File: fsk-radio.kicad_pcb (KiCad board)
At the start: 4 copper layers, 62.5 x 25 mm, 82 parts, among them IC1 STM32F4xx-QFN48, IC2 AT86RF215, IC3 LM3671, IC4 LSM6DS3, IC5 CAT24-SOT23, IC7 DPX202700DT, IC8 74AHC1G04, J1 USB_A, J2 CONN_01X14, J3 CONN_02X05, J4 RF_Shield_One_Piece, J5 u.FL, J6 u.FL, J7 SMA, X1 TXETBLSANF-26, X2 32.768kHz

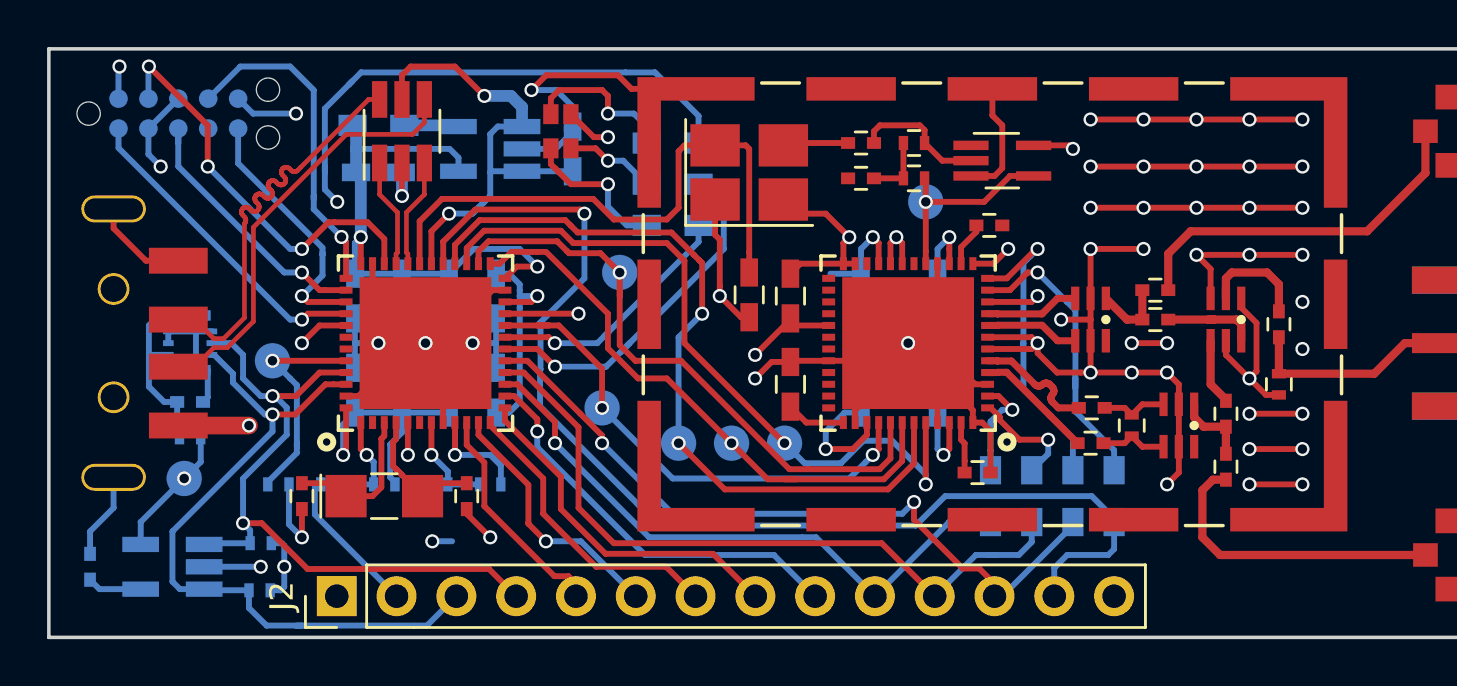
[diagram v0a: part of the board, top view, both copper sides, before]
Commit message: Cleanup silkscreen, add status LED.
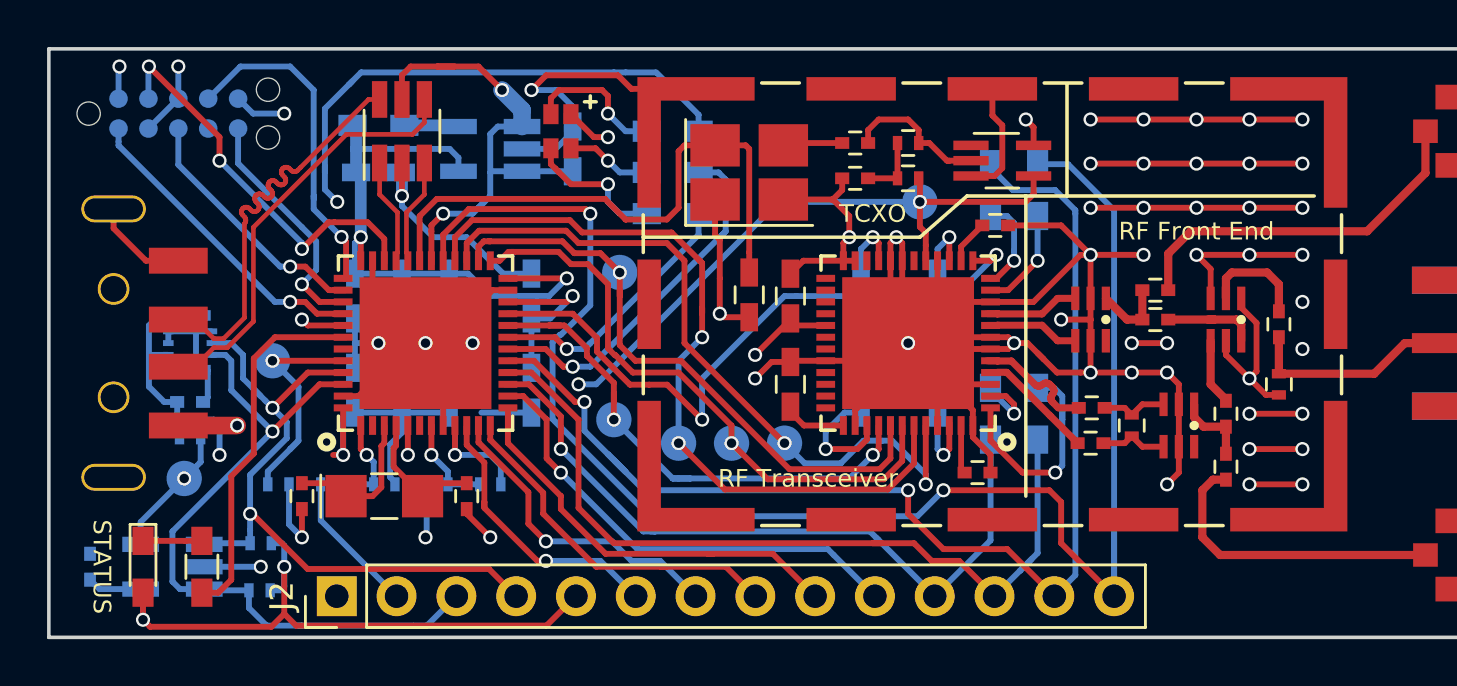
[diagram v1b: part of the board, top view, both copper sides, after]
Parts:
- added D3: LED, LEDs:LED_0603_HandSoldering, F.Cu at (101.2, 59.5)
- added R2: 270, Resistors_SMD:R_0603_HandSoldering, F.Cu at (103.8, 59.5)
- moved R15 13.5 mm to (137.2, 43.5), turned to 90 degrees
- moved R19 13.4 mm to (139.2, 43.5), turned to 90 degrees
- moved R16 3.51 mm to (139.2, 53.0)
- moved R18 3.50 mm to (137.2, 53.0)
- moved C11 1.50 mm to (117.8, 48.0), turned to 90 degrees
- moved C9 1.50 mm to (117.8, 52.0), turned to 270 degrees
- moved IRQ 0.71 mm to (121.2, 53.2)
- moved R6 0.50 mm to (123.8, 42.8)
- moved R7 0.50 mm to (123.8, 44.5)
- moved R8 0.50 mm to (123.8, 41.0)
- moved C14 0.25 mm to (131.5, 43.0)
- moved C15 0.25 mm to (131.5, 41.5)
- moved C19 0.25 mm to (137.4, 45.0)
- moved R12 0.25 mm to (133.8, 43.0)
- moved R13 0.25 mm to (133.8, 41.5)
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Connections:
- J2 pad 10: /CPU/PA5 -> /CPU/PA4
- J2 pad 11: /CPU/PA6 -> /CPU/PA5
- J2 pad 12: /CPU/PA7 -> /CPU/PA6
- J2 pad 13: /CPU/PA8 -> /CPU/PA7
- J2 pad 14: VCC -> /CPU/PA8
- J2 pad 5: /CPU/PA0 -> VCC
- J2 pad 6: /CPU/PA1 -> /CPU/PA0
- J2 pad 7: /CPU/PA2 -> /CPU/PA1
- J2 pad 8: /CPU/PA3 -> /CPU/PA2
- J2 pad 9: /CPU/PA4 -> /CPU/PA3
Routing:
- net GND: track 262.7 -> 298.2 mm, vias 53 -> 52
- net /CPU/PA7: track 31.2 -> 51.8 mm
- net /CPU/PA8: track 50.3 -> 70.4 mm, vias 1 -> 2
- net Net-(IC1-Pad42): track 0.00 -> 15.6 mm
- net /RF/FEB09: track 13.5 -> 4.18 mm
- net /RF/FEA09: track 12.6 -> 4.92 mm
- net /RF/FEA24: track 4.80 -> 9.85 mm
- net /CPU/PA6: track 30.5 -> 35.4 mm
- net /CPU/PA5: track 26.2 -> 30.9 mm
- net /CPU/PA4: track 17.4 -> 20.5 mm
- net /CPU/PA3: track 15.1 -> 17.8 mm
- net /CPU/PA2: track 12.7 -> 15.4 mm
- net Net-(C11-Pad1): track 9.60 -> 7.10 mm
- net Net-(D3-Pad1): track 0.00 -> 2.50 mm
- net Net-(IC1-Pad41): track 32.6 -> 30.1 mm
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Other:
- board text added: "A"
- board text added: "B"
- board text added: "FEx09"
- board text added: "FEx24"
- board text added: "JTAG"
- board text added: "PA7"
- board text added: "PA8"
- board text added: "RF Front End"
- board text added: "RF Transceiver"
- board text added: "STATUS"
- board text added: "TCXO"
- board text added: "https://github.com/oskirby/fsk-radio"
- board text removed: "7"
- board text removed: "8"
- board text removed: "FEA09"
- board text removed: "FEA24"
- board text removed: "FEB09"
- board text removed: "FEB24"

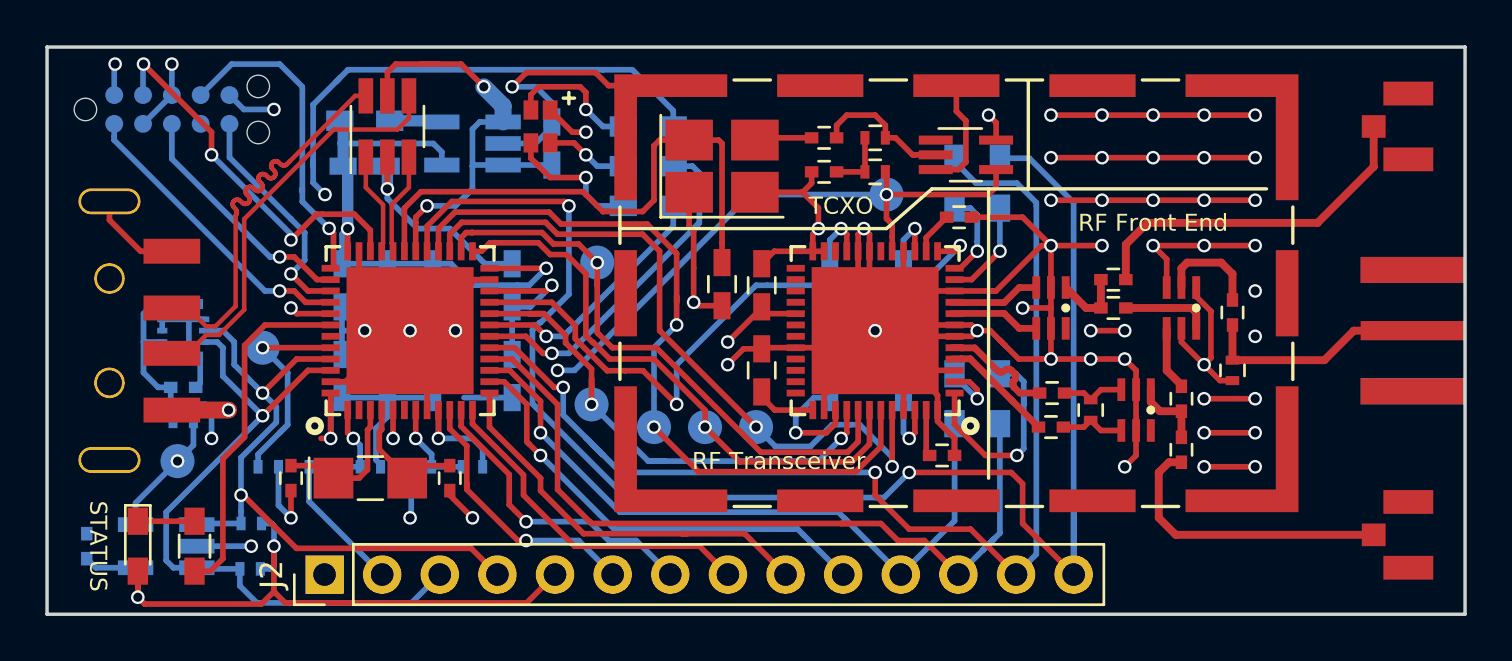
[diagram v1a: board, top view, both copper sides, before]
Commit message: Move CLKEN to BOOT1 pin to enable the TCXO during DFU boot.
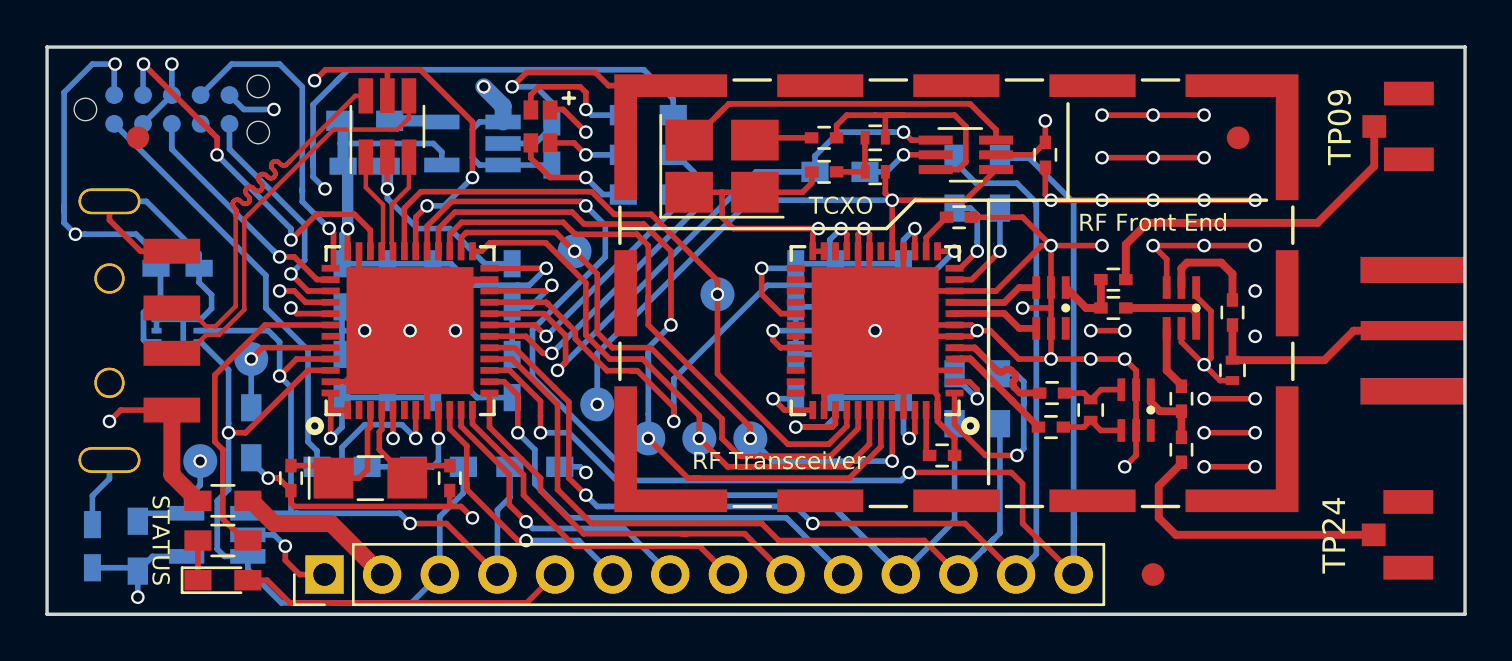
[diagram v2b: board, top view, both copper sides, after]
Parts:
- removed J5, J6: u.FL, FSK Parts:u.FL
- removed R5: 0, Resistors_SMD:R_0402
- added REF**: Fiducial_1mm_Dia_2.54mm_Outer_CopperTop, Fiducials:Fiducial_1mm_Dia_2.54mm_Outer_CopperTop, F.Cu at (101.2, 41.5)
- added REF**: Fiducial_1mm_Dia_2.54mm_Outer_CopperTop, Fiducials:Fiducial_1mm_Dia_2.54mm_Outer_CopperTop, F.Cu at (146.0, 60.8)
- added REF**: Fiducial_1mm_Dia_2.54mm_Outer_CopperTop, Fiducials:Fiducial_1mm_Dia_2.54mm_Outer_CopperTop, F.Cu at (149.8, 41.5)
- added TP09: u.FL, FSK Parts:u.FL, F.Cu at (157.3, 41.0)
- added TP24: u.FL, FSK Parts:u.FL, F.Cu at (157.2, 59.0)
- C16, C18: footprint Capacitors_SMD:C_0402 -> Capacitors_SMD:C_0603_HandSoldering
- C17: footprint Capacitors_SMD:C_0603_HandSoldering -> Capacitors_SMD:C_0402
- C21, C23: moved to B.Cu
- IC8: value 74AHC1G04 -> 74AHC2G04; footprint TO_SOT_Packages_SMD:SOT-353_SC-70-5_Handsoldering -> TO_SOT_Packages_SMD:SOT-363_SC-70-6_Handsoldering
- R1: footprint Resistors_SMD:R_0402 -> Resistors_SMD:R_0603_HandSoldering; moved to F.Cu
- R10, R11: footprint Resistors_SMD:R_0402 -> Resistors_SMD:R_0603_HandSoldering
- R14: value 4,7k -> 100k; footprint Resistors_SMD:R_0402 -> Resistors_SMD:R_0603_HandSoldering
- R3: value 0 -> 100k; footprint Resistors_SMD:R_0402 -> Resistors_SMD:R_0603_HandSoldering
- R4, R9: value 4.7k -> 100k; footprint Resistors_SMD:R_0402 -> Resistors_SMD:R_0603_HandSoldering
- moved R3 26.4 mm to (132.2, 43.0)
- moved TCXO 15.8 mm to (121.5, 53.2)
- moved C17 15.3 mm to (141.2, 42.2)
- moved R11 12.7 mm to (118.8, 56.0)
- moved R10 9.44 mm to (114.5, 56.0), turned to 0 degrees
- moved IRQ 7.37 mm to (126.8, 48.4), turned to 90 degrees
- moved R1 6.67 mm to (105.0, 57.5), turned to 180 degrees
- moved R14 5.85 mm to (101.2, 59.5), turned to 90 degrees
- moved R4 5.75 mm to (110.2, 56.0)
- moved C16 5.26 mm to (103.0, 47.2)
- moved D3 4.04 mm to (105.0, 61.0), turned to 0 degrees
- moved IC5 2.30 mm to (104.8, 59.0)
- moved R9 1.68 mm to (106.2, 54.5), turned to 270 degrees
- moved C21 1.52 mm to (130.2, 52.0)
- moved C23 1.50 mm to (130.2, 48.0), turned to 270 degrees
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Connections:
- C17 pad 2: /CPU/CLKEN -> VCC
- C4 pad 1: Net-(C4-Pad1) -> Net-(B24-Pad1)
- C4 pad 2: Net-(B24-Pad1) -> Net-(C4-Pad2)
- D2 pad 5: +5V -> Net-(D2-Pad5)
- IC1 pad 1: Net-(IC1-Pad1) -> VCC
- IC1 pad 20: /CPU/RF_IRQ -> /CPU/~CLKEN
- IC1 pad 30: +5V -> Net-(D2-Pad5)
- IC1 pad 31: /CPU/CLKEN -> /CPU/RF_IRQ
- IC8 pad 1: (no net) -> /CPU/~CLKEN
- IC8 pad 2: Net-(C15-Pad2) -> GND
- IC8 pad 3: GND -> Net-(C15-Pad2)
- J1 pad 1: +5V -> Net-(D2-Pad5)
- J3 pad 10: Net-(IC1-Pad40) -> ~NRST
- R1 pad 1: Net-(IC1-Pad1) -> +5V
- R1 pad 2: VCC -> Net-(D2-Pad5)
- R3 pad 1: Net-(IC1-Pad1) -> GND
- R3 pad 2: +5V -> /CPU/~CLKEN
- X1 pad 4: /CPU/CLKEN -> Net-(IC8-Pad6)
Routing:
- net Net-(D2-Pad5): track 0.00 -> 42.8 mm, vias 0 -> 4
- net GND: track 298.2 -> 328.8 mm, vias 52 -> 48
- net /CPU/~CLKEN: track 0.00 -> 27.5 mm, vias 0 -> 2
- net Net-(IC1-Pad40): track 29.6 -> 2.46 mm, vias 2 -> 1
- net /CPU/CLKEN: track 24.7 -> 0.00 mm
- net VCC: track 118.5 -> 142.3 mm
- net ~NRST: track 4.28 -> 26.1 mm
- net Net-(IC8-Pad6): track 0.00 -> 15.5 mm
- net +5V: track 62.8 -> 48.6 mm, vias 3 -> 1
- net Net-(C4-Pad1): track 13.0 -> 0.00 mm
- net Net-(C4-Pad2): track 0.00 -> 12.6 mm
- net /CPU/RF_IRQ: track 22.7 -> 29.7 mm, vias 2 -> 1
- net Net-(C15-Pad2): track 6.15 -> 11.5 mm
- net Net-(IC1-Pad1): track 4.15 -> 0.00 mm, vias 1 -> 0
- net Net-(BOOT1-Pad1): track 9.77 -> 5.86 mm
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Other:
- rule pad_to_mask_clearance: 0.2 -> 0.05
- board text added: "EEPROM"

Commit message: Release for manufacturing.
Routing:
- net VCC: track 142.3 -> 139.9 mm
- net GND: track 328.8 -> 330.0 mm, vias 48 -> 49
- net /CPU/SPI_CLK: track 26.5 -> 27.7 mm
- net /CPU/RF_IRQ: track 29.7 -> 30.3 mm
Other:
- board text added: "LED1"
- board text added: "LED2"
- board text removed: "STATUS"
